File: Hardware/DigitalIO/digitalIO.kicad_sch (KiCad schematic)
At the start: 0 parts

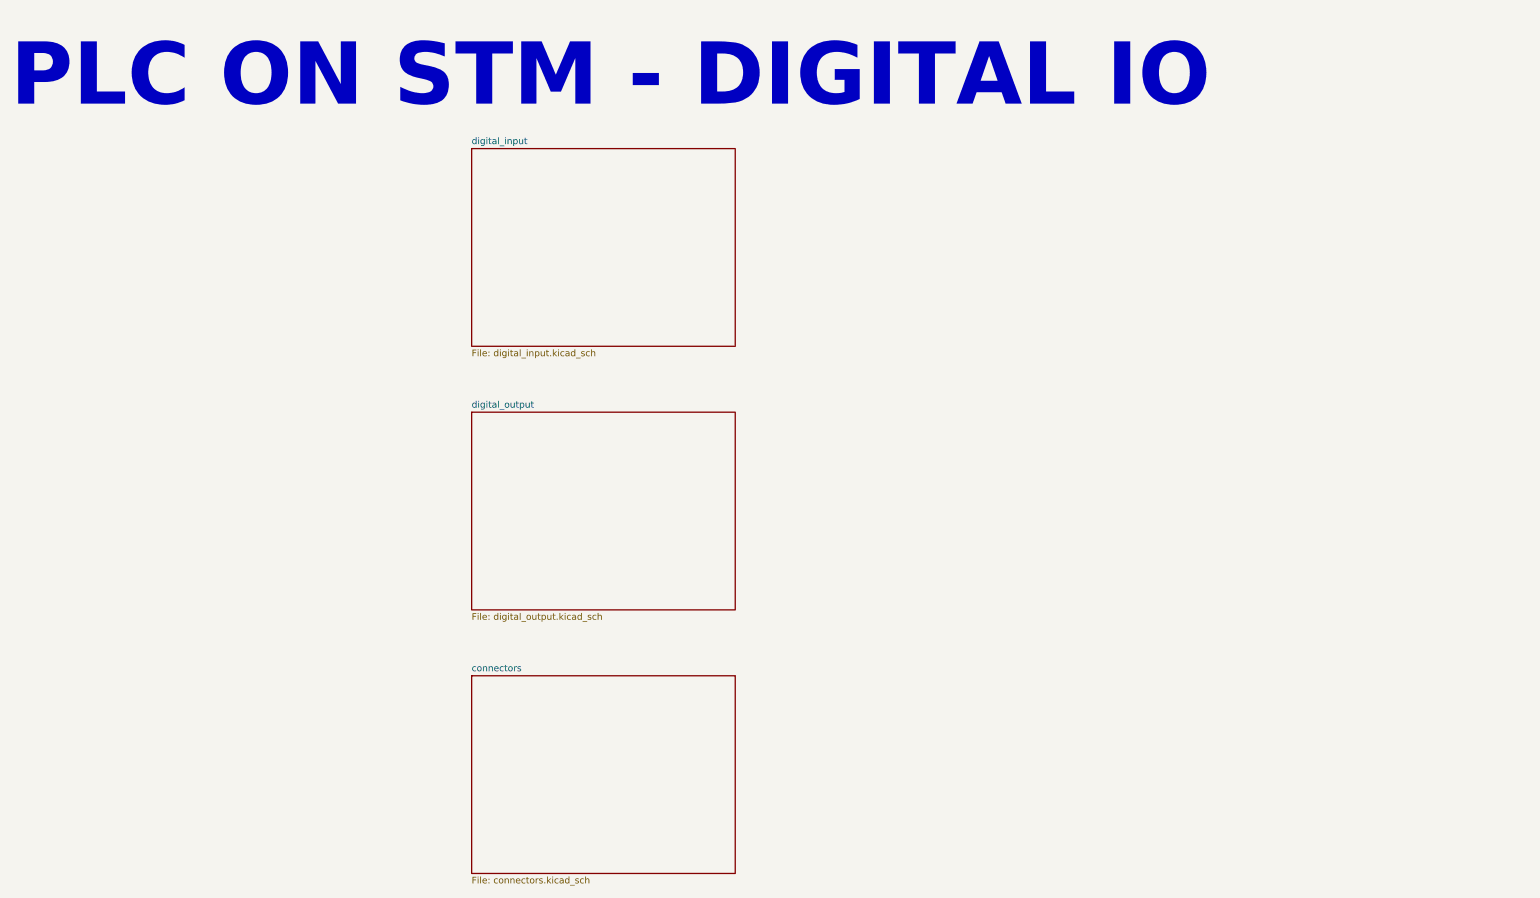
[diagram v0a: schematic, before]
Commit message: schematic update - all pcbs
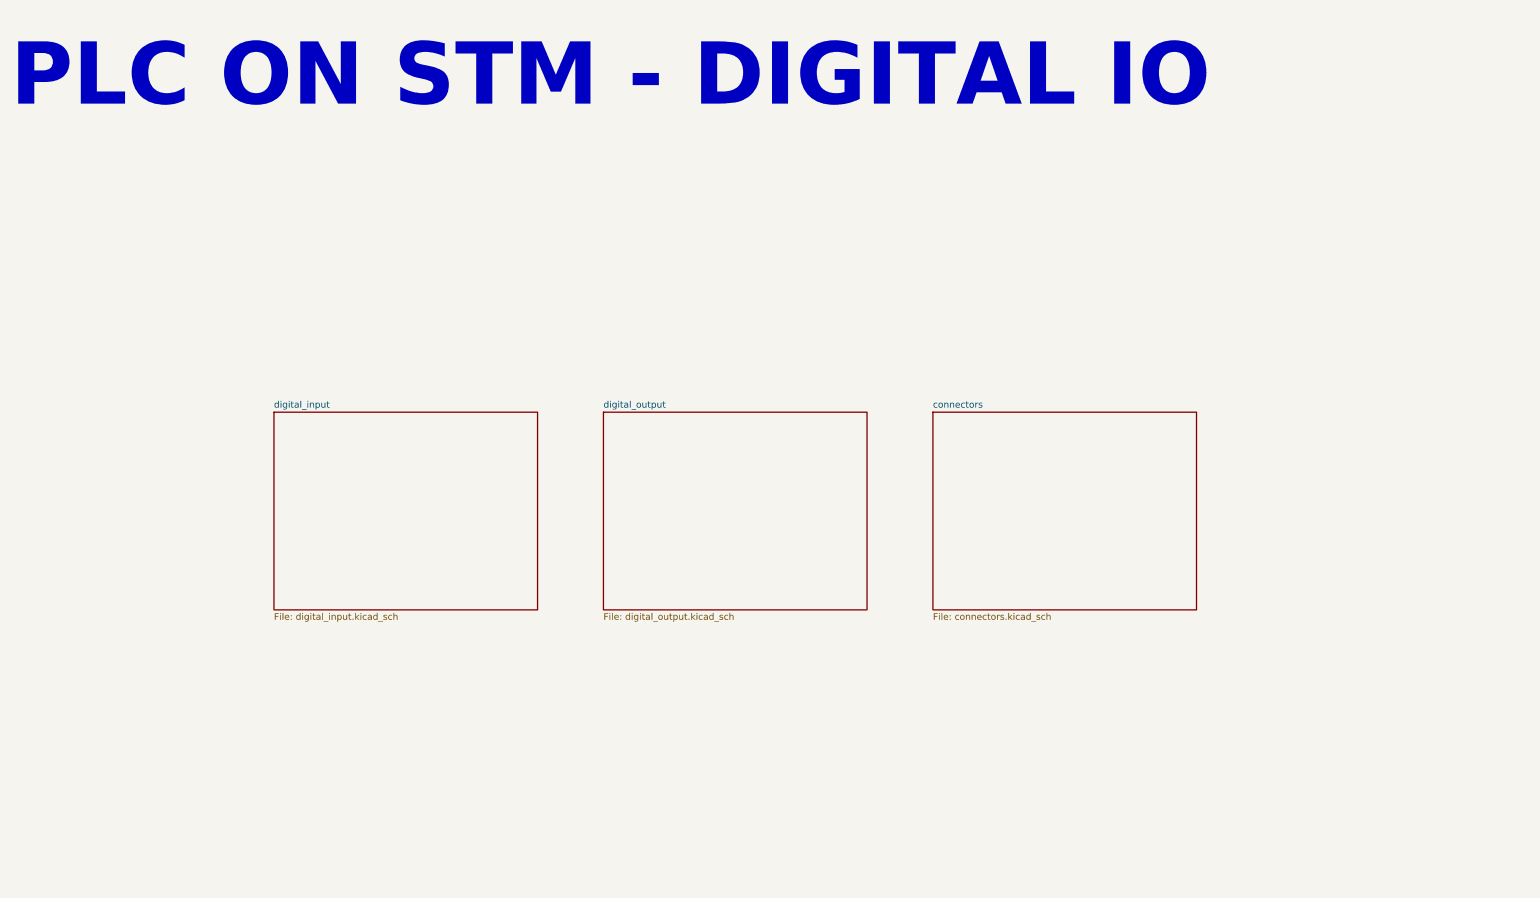
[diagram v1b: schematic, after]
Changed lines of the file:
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@@
 	)
 	(sheet
-		(at 101.6 88.9)
+		(at 127 88.9)
 		(size 50.8 38.1)
 		(exclude_from_sim no)
@@
 		)
 		(property "Sheetname" "digital_output"
-			(at 101.6 88.1884 0)
+			(at 127 88.1884 0)
 			(effects
 				(font
@@
 		)
 		(property "Sheetfile" "digital_output.kicad_sch"
-			(at 101.6 127.5846 0)
+			(at 127 127.5846 0)
 			(effects
 				(font
@@
 	)
 	(sheet
-		(at 101.6 139.7)
+		(at 190.5 88.9)
 		(size 50.8 38.1)
 		(exclude_from_sim no)
@@
 		)
 		(property "Sheetname" "connectors"
-			(at 101.6 138.9884 0)
+			(at 190.5 88.1884 0)
 			(effects
 				(font
@@
 		)
 		(property "Sheetfile" "connectors.kicad_sch"
-			(at 101.6 178.3846 0)
+			(at 190.5 127.5846 0)
 			(effects
 				(font
@@
 	)
 	(sheet
-		(at 101.6 38.1)
+		(at 63.5 88.9)
 		(size 50.8 38.1)
 		(exclude_from_sim no)
@@
 		)
 		(property "Sheetname" "digital_input"
-			(at 101.6 37.3884 0)
+			(at 63.5 88.1884 0)
 			(effects
 				(font
@@
 		)
 		(property "Sheetfile" "digital_input.kicad_sch"
-			(at 101.6 76.7846 0)
+			(at 63.5 127.5846 0)
 			(effects
 				(font
